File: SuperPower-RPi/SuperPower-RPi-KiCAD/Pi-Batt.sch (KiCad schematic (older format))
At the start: 9 parts, among them J2 Conn_01x02, J4 Conn_01x02, Q1 SSM3J328R, Q2 Q_NPN_BCE

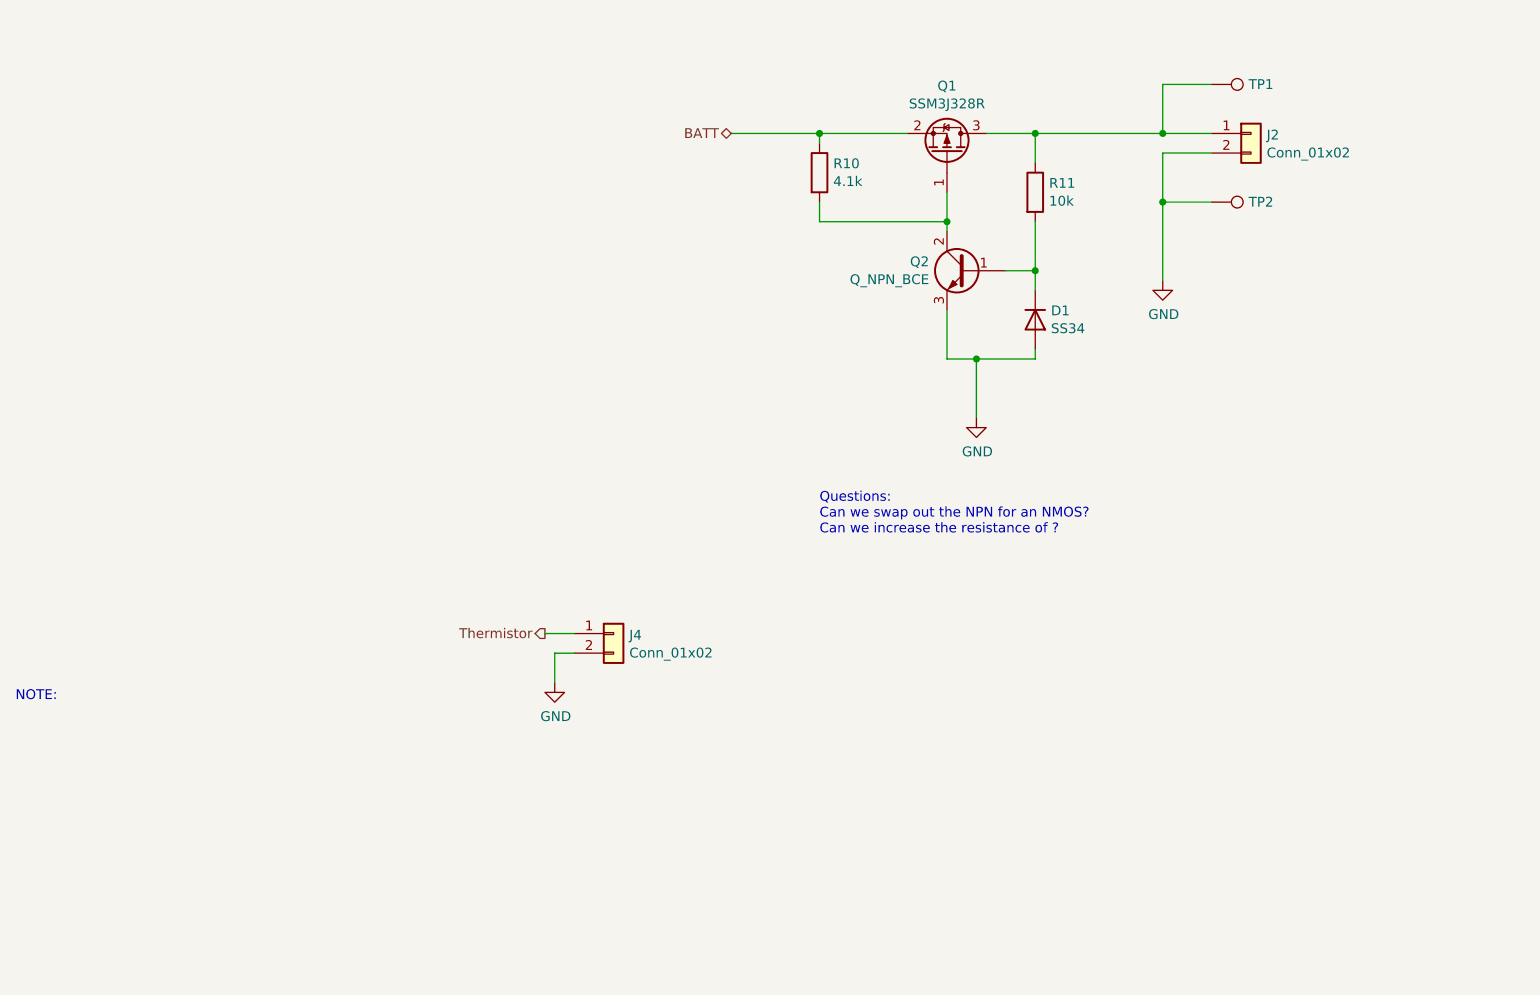
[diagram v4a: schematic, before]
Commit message: Component Updates.
Redid battery reverse polarty circuit to use an NMOS.

Added note for important parameters in overvoltage protection circuit.

(cherry picked from commit 69b0d79b222f07f7c875c3ca5cc6bb34230cf411)
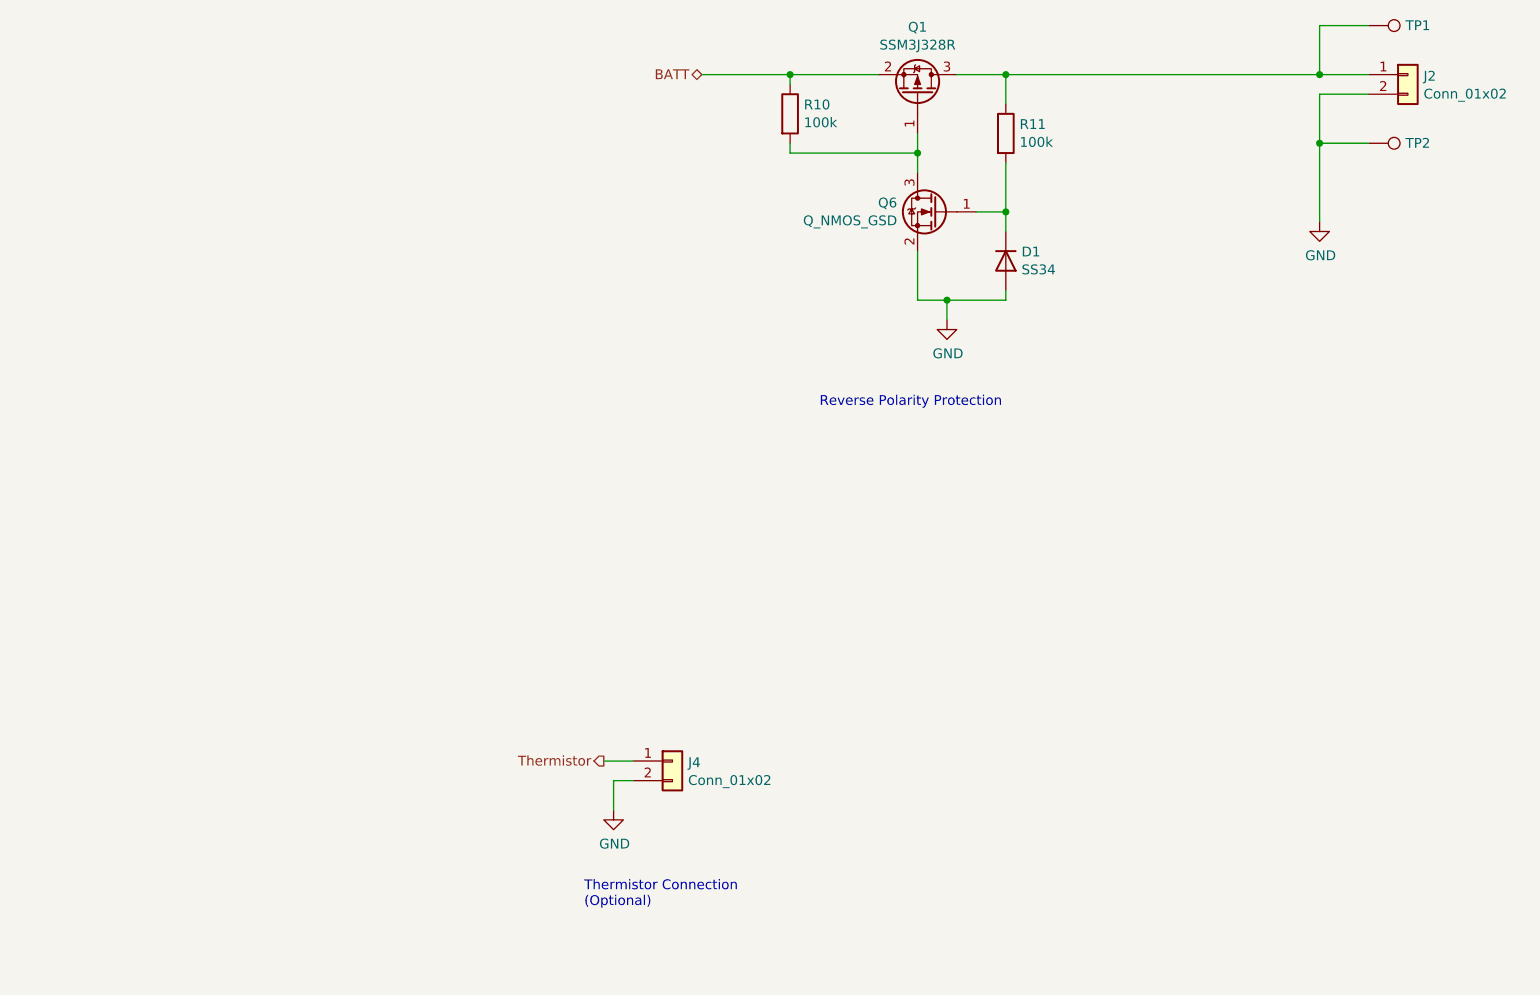
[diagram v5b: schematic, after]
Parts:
- removed Q2: Q_NPN_BCE, symbol Device:Q_NPN_BCE
- added Q6: Q_NMOS_GSD, symbol Device:Q_NMOS_GSD
- R10: value 4.1k -> 100k; Digi-Key PN (none) -> 311-100KHRCT-ND; Mfg (none) -> Yageo; Mfg PN (none) -> RC0603FR-07100KL
- R11: value 10k -> 100k; Digi-Key PN (none) -> 311-100KHRCT-ND; Mfg (none) -> Yageo; Mfg PN (none) -> RC0603FR-07100KL
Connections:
- net GND: now also Q6.2 (S)
- net at D1.1 (K), R11.2: now also Q6.1 (G)
- net at Q1.1 (G), R10.2: now also Q6.3 (D)
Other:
- note added: "Reverse Polarity Protection"
- note added: "Thermistor Connection\n(Optional)"
- note removed: "NOTE:\n"
- note removed: "Questions:\nCan we swap out the NPN for an NMOS?\nCan we increase the resistance of ?"
- moved on the sheet: D1, J2, J4, Q1, R10, R11, TP1, TP2
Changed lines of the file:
@@
 Comment4 ""
 $EndDescr
-Text HLabel 4700 2700 0    50   BiDi ~ 0
+Text HLabel 4550 2400 0    50   BiDi ~ 0
 BATT
-Text Notes 1050 5600 0    50   ~ 0
-NOTE:\n
 $Comp
 L Connector_Generic:Conn_01x02 J2
 U 1 1 5F701F7D
-P 7350 2700
-F 0 "J2" H 7430 2692 50  0000 L CNN
-F 1 "Conn_01x02" H 7430 2601 50  0000 L CNN
-F 2 "" H 7350 2700 50  0001 C CNN
-F 3 "~" H 7350 2700 50  0001 C CNN
-	1    7350 2700
+P 8150 2400
+F 0 "J2" H 8230 2392 50  0000 L CNN
+F 1 "Conn_01x02" H 8230 2301 50  0000 L CNN
+F 2 "" H 8150 2400 50  0001 C CNN
+F 3 "~" H 8150 2400 50  0001 C CNN
+	1    8150 2400
 	1    0    0    -1
 $EndComp
@@
 L Device:D D1
 U 1 1 5F702A8B
-P 6250 3650
-F 0 "D1" V 6204 3730 50  0000 L CNN
-F 1 "SS34" V 6295 3730 50  0000 L CNN
-F 2 "" H 6250 3650 50  0001 C CNN
-F 3 "~" H 6250 3650 50  0001 C CNN
-	1    6250 3650
+P 6100 3350
+F 0 "D1" V 6054 3430 50  0000 L CNN
+F 1 "SS34" V 6145 3430 50  0000 L CNN
+F 2 "" H 6100 3350 50  0001 C CNN
+F 3 "~" H 6100 3350 50  0001 C CNN
+	1    6100 3350
 	0    1    1    0
 $EndComp
@@
 L power:GND #PWR0103
 U 1 1 5F703173
-P 5950 4150
-F 0 "#PWR0103" H 5950 3900 50  0001 C CNN
-F 1 "GND" H 5955 3977 50  0000 C CNN
-F 2 "" H 5950 4150 50  0001 C CNN
-F 3 "" H 5950 4150 50  0001 C CNN
-	1    5950 4150
+P 5800 3650
+F 0 "#PWR0103" H 5800 3400 50  0001 C CNN
+F 1 "GND" H 5805 3477 50  0000 C CNN
+F 2 "" H 5800 3650 50  0001 C CNN
+F 3 "" H 5800 3650 50  0001 C CNN
+	1    5800 3650
 	1    0    0    -1
 $EndComp
@@
 L Device:R R11
 U 1 1 5F7036D1
-P 6250 3000
-F 0 "R11" H 6320 3046 50  0000 L CNN
-F 1 "10k" H 6320 2955 50  0000 L CNN
-F 2 "Resistor_SMD:R_0603_1608Metric" V 6180 3000 50  0001 C CNN
-F 3 "~" H 6250 3000 50  0001 C CNN
-	1    6250 3000
+P 6100 2700
+F 0 "R11" H 6170 2746 50  0000 L CNN
+F 1 "100k" H 6170 2655 50  0000 L CNN
+F 2 "Resistor_SMD:R_0603_1608Metric" V 6030 2700 50  0001 C CNN
+F 3 "~" H 6100 2700 50  0001 C CNN
+F 4 "311-100KHRCT-ND" H 6100 2700 50  0001 C CNN "Digi-Key PN"
+F 5 "Yageo" H 6100 2700 50  0001 C CNN "Mfg"
+F 6 "RC0603FR-07100KL" H 6100 2700 50  0001 C CNN "Mfg PN"
+	1    6100 2700
 	1    0    0    -1
 $EndComp
@@
 L Device:Q_PMOS_GSD Q1
 U 1 1 5F704F9B
-P 5800 2800
-F 0 "Q1" V 6142 2800 50  0000 C CNN
-F 1 "SSM3J328R" V 6051 2800 50  0000 C CNN
-F 2 "" H 6000 2900 50  0001 C CNN
-F 3 "~" H 5800 2800 50  0001 C CNN
-	1    5800 2800
+P 5650 2500
+F 0 "Q1" V 5992 2500 50  0000 C CNN
+F 1 "SSM3J328R" V 5901 2500 50  0000 C CNN
+F 2 "" H 5850 2600 50  0001 C CNN
+F 3 "~" H 5650 2500 50  0001 C CNN
+	1    5650 2500
 	0    1    -1   0
 $EndComp
 Wire Wire Line
-	6250 2700 6250 2850
-Wire Wire Line
-	6000 2700 6250 2700
-Connection ~ 6250 2700
-Wire Wire Line
-	6250 2700 6900 2700
-$Comp
-L Device:Q_NPN_BCE Q2
-U 1 1 5F708549
-P 5900 3400
-F 0 "Q2" H 6091 3446 50  0000 L CNN
-F 1 "Q_NPN_BCE" H 6091 3355 50  0000 L CNN
-F 2 "" H 6100 3500 50  0001 C CNN
-F 3 "~" H 5900 3400 50  0001 C CNN
-	1    5900 3400
-	-1   0    0    -1
-$EndComp
-Wire Wire Line
-	5800 3600 5800 3850
-Wire Wire Line
-	5800 3850 5950 3850
-Wire Wire Line
-	6250 3850 6250 3800
-Wire Wire Line
-	6250 3500 6250 3400
-Wire Wire Line
-	6100 3400 6250 3400
-Connection ~ 6250 3400
-Wire Wire Line
-	6250 3400 6250 3150
-Wire Wire Line
-	5800 3200 5800 3150
-Wire Wire Line
-	5950 4150 5950 3850
-Connection ~ 5950 3850
-Wire Wire Line
-	5950 3850 6250 3850
+	6100 2400 6100 2550
+Wire Wire Line
+	5850 2400 6100 2400
+Wire Wire Line
+	5650 3300 5650 3550
+Wire Wire Line
+	5650 3550 5800 3550
+Wire Wire Line
+	6100 3550 6100 3500
+Wire Wire Line
+	6100 3200 6100 3100
+Wire Wire Line
+	5950 3100 6100 3100
+Connection ~ 6100 3100
+Wire Wire Line
+	6100 3100 6100 2850
+Wire Wire Line
+	5650 2900 5650 2800
+Wire Wire Line
+	5800 3650 5800 3550
+Connection ~ 5800 3550
+Wire Wire Line
+	5800 3550 6100 3550
 $Comp
 L Device:R R10
 U 1 1 5F709FD7
-P 5150 2900
-F 0 "R10" H 5220 2946 50  0000 L CNN
-F 1 "4.1k" H 5220 2855 50  0000 L CNN
-F 2 "Resistor_SMD:R_0603_1608Metric" V 5080 2900 50  0001 C CNN
-F 3 "~" H 5150 2900 50  0001 C CNN
-	1    5150 2900
-	1    0    0    -1
-$EndComp
-Wire Wire Line
-	5150 2750 5150 2700
-Wire Wire Line
-	5150 2700 5600 2700
-Wire Wire Line
-	5150 3050 5150 3150
-Wire Wire Line
-	5150 3150 5800 3150
-Connection ~ 5800 3150
-Wire Wire Line
-	5800 3150 5800 3000
-Wire Wire Line
-	4700 2700 5150 2700
-Connection ~ 5150 2700
-Text Notes 5150 4750 0    50   ~ 0
-Questions:\nCan we swap out the NPN for an NMOS?\nCan we increase the resistance of ?
+P 5000 2600
+F 0 "R10" H 5070 2646 50  0000 L CNN
+F 1 "100k" H 5070 2555 50  0000 L CNN
+F 2 "Resistor_SMD:R_0603_1608Metric" V 4930 2600 50  0001 C CNN
+F 3 "~" H 5000 2600 50  0001 C CNN
+F 4 "311-100KHRCT-ND" H 5000 2600 50  0001 C CNN "Digi-Key PN"
+F 5 "Yageo" H 5000 2600 50  0001 C CNN "Mfg"
+F 6 "RC0603FR-07100KL" H 5000 2600 50  0001 C CNN "Mfg PN"
+	1    5000 2600
+	1    0    0    -1
+$EndComp
+Wire Wire Line
+	5000 2450 5000 2400
+Wire Wire Line
+	5000 2400 5450 2400
+Wire Wire Line
+	5000 2750 5000 2800
+Wire Wire Line
+	5000 2800 5650 2800
+Connection ~ 5650 2800
+Wire Wire Line
+	5650 2800 5650 2700
+Wire Wire Line
+	4550 2400 5000 2400
+Connection ~ 5000 2400
 $Comp
 L power:GND #PWR0104
 U 1 1 5F70F58A
-P 6900 3450
-F 0 "#PWR0104" H 6900 3200 50  0001 C CNN
-F 1 "GND" H 6905 3277 50  0000 C CNN
-F 2 "" H 6900 3450 50  0001 C CNN
-F 3 "" H 6900 3450 50  0001 C CNN
-	1    6900 3450
+P 7700 3150
+F 0 "#PWR0104" H 7700 2900 50  0001 C CNN
+F 1 "GND" H 7705 2977 50  0000 C CNN
+F 2 "" H 7700 3150 50  0001 C CNN
+F 3 "" H 7700 3150 50  0001 C CNN
+	1    7700 3150
 	1    0    0    -1
 $EndComp
@@
 L Connector:TestPoint TP2
 U 1 1 5F70FBD7
-P 7150 3050
-F 0 "TP2" V 7150 3238 50  0000 L CNN
-F 1 "TestPoint" V 7195 3238 50  0001 L CNN
-F 2 "" H 7350 3050 50  0001 C CNN
-F 3 "~" H 7350 3050 50  0001 C CNN
-	1    7150 3050
+P 7950 2750
+F 0 "TP2" V 7950 2938 50  0000 L CNN
+F 1 "TestPoint" V 7995 2938 50  0001 L CNN
+F 2 "" H 8150 2750 50  0001 C CNN
+F 3 "~" H 8150 2750 50  0001 C CNN
+	1    7950 2750
 	0    1    1    0
 $EndComp
@@
 L Connector:TestPoint TP1
 U 1 1 5F710403
-P 7150 2450
-F 0 "TP1" V 7150 2638 50  0000 L CNN
-F 1 "TestPoint" V 7195 2638 50  0001 L CNN
-F 2 "" H 7350 2450 50  0001 C CNN
-F 3 "~" H 7350 2450 50  0001 C CNN
-	1    7150 2450
+P 7950 2150
+F 0 "TP1" V 7950 2338 50  0000 L CNN
+F 1 "TestPoint" V 7995 2338 50  0001 L CNN
+F 2 "" H 8150 2150 50  0001 C CNN
+F 3 "~" H 8150 2150 50  0001 C CNN
+	1    7950 2150
 	0    1    1    0
 $EndComp
 Wire Wire Line
-	7150 2450 6900 2450
-Wire Wire Line
-	6900 2450 6900 2700
-Connection ~ 6900 2700
-Wire Wire Line
-	6900 2700 7150 2700
-Wire Wire Line
-	7150 3050 6900 3050
-Wire Wire Line
-	6900 3050 6900 3450
-Wire Wire Line
-	6900 3050 6900 2800
-Wire Wire Line
-	6900 2800 7150 2800
-Connection ~ 6900 3050
-Text HLabel 3750 5250 0    50   Output ~ 0
+	7950 2150 7700 2150
+Wire Wire Line
+	7700 2150 7700 2400
+Connection ~ 7700 2400
+Wire Wire Line
+	7700 2400 7950 2400
+Wire Wire Line
+	7950 2750 7700 2750
+Wire Wire Line
+	7700 2750 7700 3150
+Wire Wire Line
+	7700 2750 7700 2500
+Wire Wire Line
+	7700 2500 7950 2500
+Connection ~ 7700 2750
+Text HLabel 4050 5900 0    50   Output ~ 0
 Thermistor
 $Comp
 L Connector_Generic:Conn_01x02 J4
 U 1 1 5F7ACDE2
-P 4100 5250
-F 0 "J4" H 4180 5242 50  0000 L CNN
-F 1 "Conn_01x02" H 4180 5151 50  0000 L CNN
-F 2 "" H 4100 5250 50  0001 C CNN
-F 3 "~" H 4100 5250 50  0001 C CNN
-	1    4100 5250
-	1    0    0    -1
-$EndComp
-Wire Wire Line
-	3900 5250 3750 5250
+P 4400 5900
+F 0 "J4" H 4480 5892 50  0000 L CNN
+F 1 "Conn_01x02" H 4480 5801 50  0000 L CNN
+F 2 "" H 4400 5900 50  0001 C CNN
+F 3 "~" H 4400 5900 50  0001 C CNN
+	1    4400 5900
+	1    0    0    -1
+$EndComp
+Wire Wire Line
+	4200 5900 4050 5900
 $Comp
 L power:GND #PWR015
 U 1 1 5F7AD85C
-P 3800 5500
-F 0 "#PWR015" H 3800 5250 50  0001 C CNN
-F 1 "GND" H 3805 5327 50  0000 C CNN
-F 2 "" H 3800 5500 50  0001 C CNN
-F 3 "" H 3800 5500 50  0001 C CNN
-	1    3800 5500
-	1    0    0    -1
-$EndComp
-Wire Wire Line
-	3800 5500 3800 5350
-Wire Wire Line
-	3800 5350 3900 5350
+P 4100 6150
+F 0 "#PWR015" H 4100 5900 50  0001 C CNN
+F 1 "GND" H 4105 5977 50  0000 C CNN
+F 2 "" H 4100 6150 50  0001 C CNN
+F 3 "" H 4100 6150 50  0001 C CNN
+	1    4100 6150
+	1    0    0    -1
+$EndComp
+Wire Wire Line
+	4100 6150 4100 6000
+Wire Wire Line
+	4100 6000 4200 6000
+$Comp
+L Device:Q_NMOS_GSD Q?
+U 1 1 5FA86C0C
+P 5750 3100
+AR Path="/5F6AC517/5FA86C0C" Ref="Q?"  Part="1"
+AR Path="/5F6AC644/5FA86C0C" Ref="Q6"  Part="1"
+F 0 "Q6" H 5954 3146 50  0000 L CNN
+F 1 "Q_NMOS_GSD" H 5954 3055 50  0000 L CNN
+F 2 "" H 5950 3200 50  0001 C CNN
+F 3 "~" H 5750 3100 50  0001 C CNN
+	1    5750 3100
+	-1   0    0    -1
+$EndComp
+Wire Wire Line
+	6100 2400 7700 2400
+Connection ~ 6100 2400
+Text Notes 5150 4100 0    50   ~ 0
+Reverse Polarity Protection
+Text Notes 3950 6650 0    50   ~ 0
+Thermistor Connection\n(Optional)
 $EndSCHEMATC

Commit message: Added local footprint library, and associated components.
(cherry picked from commit 78b1abfd5fe55b90039e798d35239acda24b0417)
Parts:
- D1: footprint (none) -> Diode_SMD:D_SOD-123
- Q1, Q6: footprint (none) -> Package_TO_SOT_SMD:SOT-23; Mfg (none) -> FIX FOOTPRINT
- TP1, TP2: value TestPoint -> DNP; footprint (none) -> Connector_Wire:SolderWire-1.5sqmm_1x01_D1.7mm_OD3.9mm
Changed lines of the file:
@@
 F 0 "D1" V 6054 3430 50  0000 L CNN
 F 1 "SS34" V 6145 3430 50  0000 L CNN
-F 2 "" H 6100 3350 50  0001 C CNN
+F 2 "Diode_SMD:D_SOD-123" H 6100 3350 50  0001 C CNN
 F 3 "~" H 6100 3350 50  0001 C CNN
 	1    6100 3350
@@
 F 0 "Q1" V 5992 2500 50  0000 C CNN
 F 1 "SSM3J328R" V 5901 2500 50  0000 C CNN
-F 2 "" H 5850 2600 50  0001 C CNN
+F 2 "Package_TO_SOT_SMD:SOT-23" H 5850 2600 50  0001 C CNN
 F 3 "~" H 5650 2500 50  0001 C CNN
+F 4 "FIX FOOTPRINT" H 5650 2500 50  0001 C CNN "Mfg"
 	1    5650 2500
 	0    1    -1   0
@@
 P 7950 2750
 F 0 "TP2" V 7950 2938 50  0000 L CNN
-F 1 "TestPoint" V 7995 2938 50  0001 L CNN
-F 2 "" H 8150 2750 50  0001 C CNN
+F 1 "DNP" V 7995 2938 50  0001 L CNN
+F 2 "Connector_Wire:SolderWire-1.5sqmm_1x01_D1.7mm_OD3.9mm" H 8150 2750 50  0001 C CNN
 F 3 "~" H 8150 2750 50  0001 C CNN
 	1    7950 2750
@@
 P 7950 2150
 F 0 "TP1" V 7950 2338 50  0000 L CNN
-F 1 "TestPoint" V 7995 2338 50  0001 L CNN
-F 2 "" H 8150 2150 50  0001 C CNN
+F 1 "DNP" V 7995 2338 50  0001 L CNN
+F 2 "Connector_Wire:SolderWire-1.5sqmm_1x01_D1.7mm_OD3.9mm" H 8150 2150 50  0001 C CNN
 F 3 "~" H 8150 2150 50  0001 C CNN
 	1    7950 2150
@@
 F 0 "Q6" H 5954 3146 50  0000 L CNN
 F 1 "Q_NMOS_GSD" H 5954 3055 50  0000 L CNN
-F 2 "" H 5950 3200 50  0001 C CNN
+F 2 "Package_TO_SOT_SMD:SOT-23" H 5950 3200 50  0001 C CNN
 F 3 "~" H 5750 3100 50  0001 C CNN
+F 4 "FIX FOOTPRINT" H 5750 3100 50  0001 C CNN "Mfg"
 	1    5750 3100
 	-1   0    0    -1

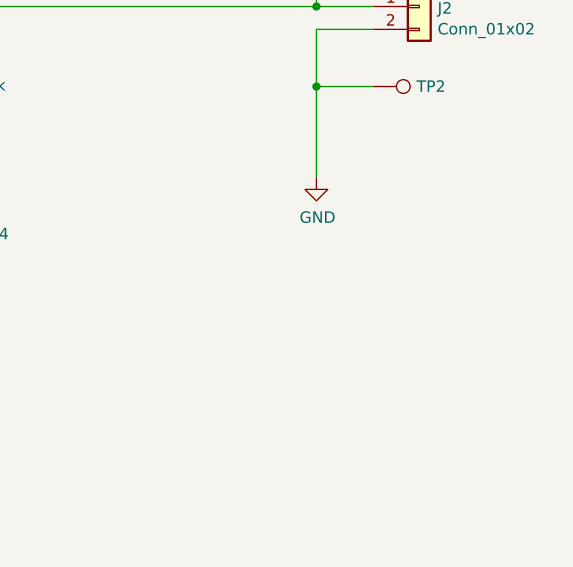
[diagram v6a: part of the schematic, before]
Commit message: Added temporary footprints and imported into pcb.
(cherry picked from commit a685dfc635e321a03e1c1fd194e70e2193ef2183)
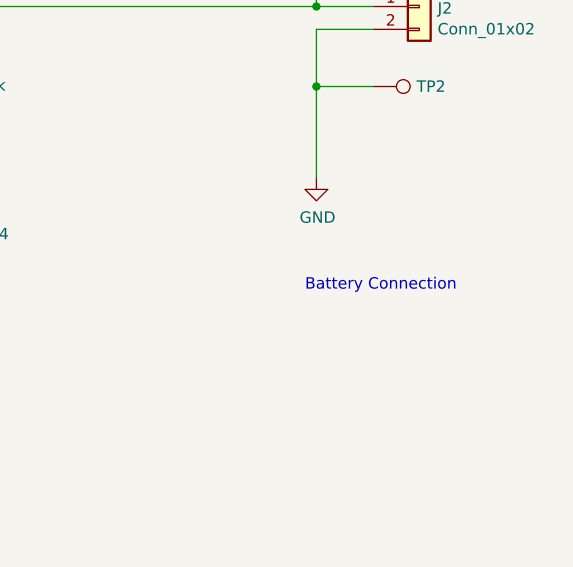
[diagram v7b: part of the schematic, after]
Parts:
- D1: Mfg (none) -> FIX FOOTPRINT
- J2: footprint (none) -> Connector_JST:JST_PH_B2B-PH-K_1x02_P2.00mm_Vertical; Mfg (none) -> FIX FOOTPRINT
- J4: footprint (none) -> Connector_PinHeader_2.00mm:PinHeader_1x02_P2.00mm_Vertical
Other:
- note added: "Battery Connection"
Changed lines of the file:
@@
 F 0 "J2" H 8230 2392 50  0000 L CNN
 F 1 "Conn_01x02" H 8230 2301 50  0000 L CNN
-F 2 "" H 8150 2400 50  0001 C CNN
+F 2 "Connector_JST:JST_PH_B2B-PH-K_1x02_P2.00mm_Vertical" H 8150 2400 50  0001 C CNN
 F 3 "~" H 8150 2400 50  0001 C CNN
+F 4 "FIX FOOTPRINT" H 8150 2400 50  0001 C CNN "Mfg"
 	1    8150 2400
 	1    0    0    -1
@@
 F 2 "Diode_SMD:D_SOD-123" H 6100 3350 50  0001 C CNN
 F 3 "~" H 6100 3350 50  0001 C CNN
+F 4 "FIX FOOTPRINT" H 6100 3350 50  0001 C CNN "Mfg"
 	1    6100 3350
 	0    1    1    0
@@
 F 0 "J4" H 4480 5892 50  0000 L CNN
 F 1 "Conn_01x02" H 4480 5801 50  0000 L CNN
-F 2 "" H 4400 5900 50  0001 C CNN
+F 2 "Connector_PinHeader_2.00mm:PinHeader_1x02_P2.00mm_Vertical" H 4400 5900 50  0001 C CNN
 F 3 "~" H 4400 5900 50  0001 C CNN
 	1    4400 5900
@@
 Text Notes 3950 6650 0    50   ~ 0
 Thermistor Connection\n(Optional)
+Text Notes 7650 3650 0    50   ~ 0
+Battery Connection
 $EndSCHEMATC
